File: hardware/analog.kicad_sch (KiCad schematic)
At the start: 23 parts

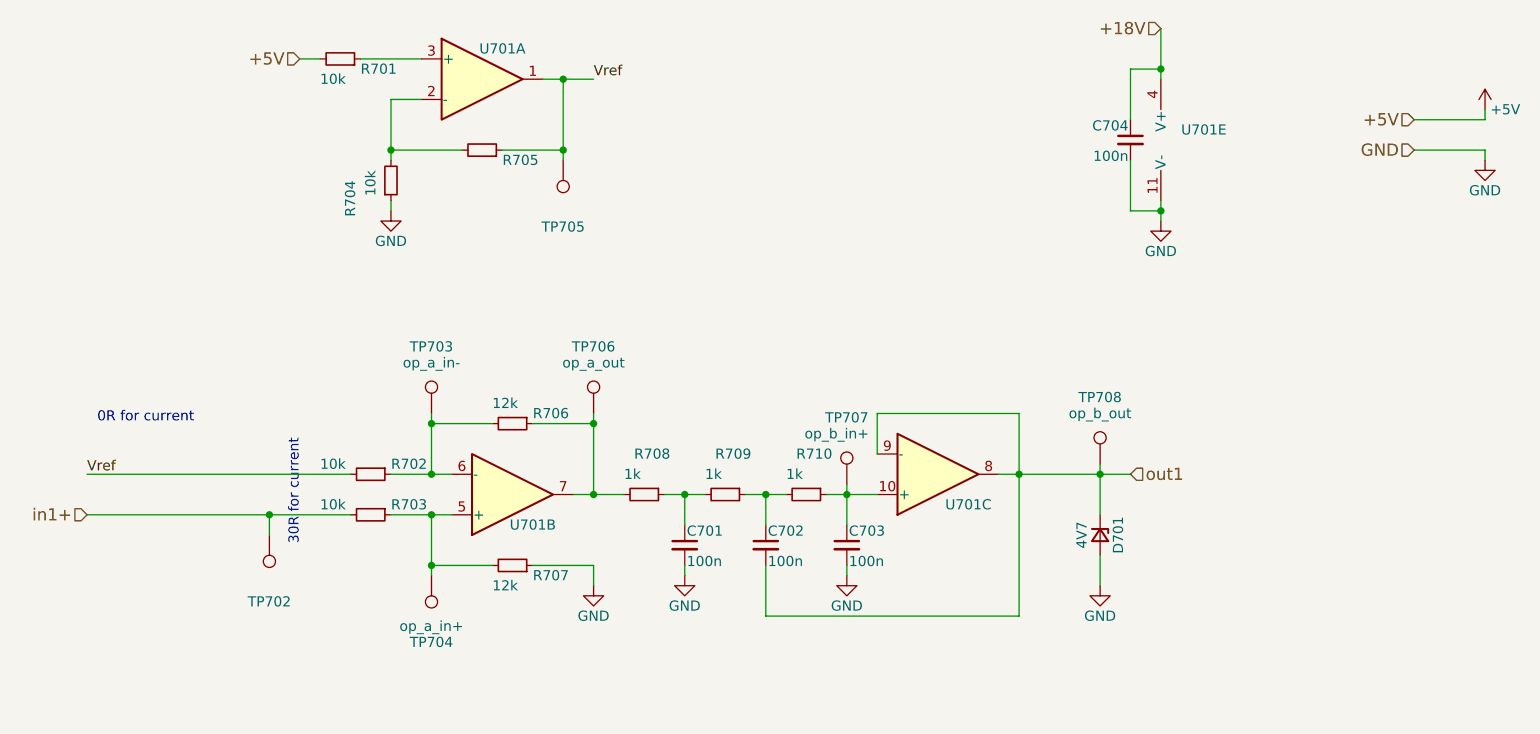
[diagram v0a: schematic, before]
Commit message: Adjusted analog, now using INA826. Simulations updated.
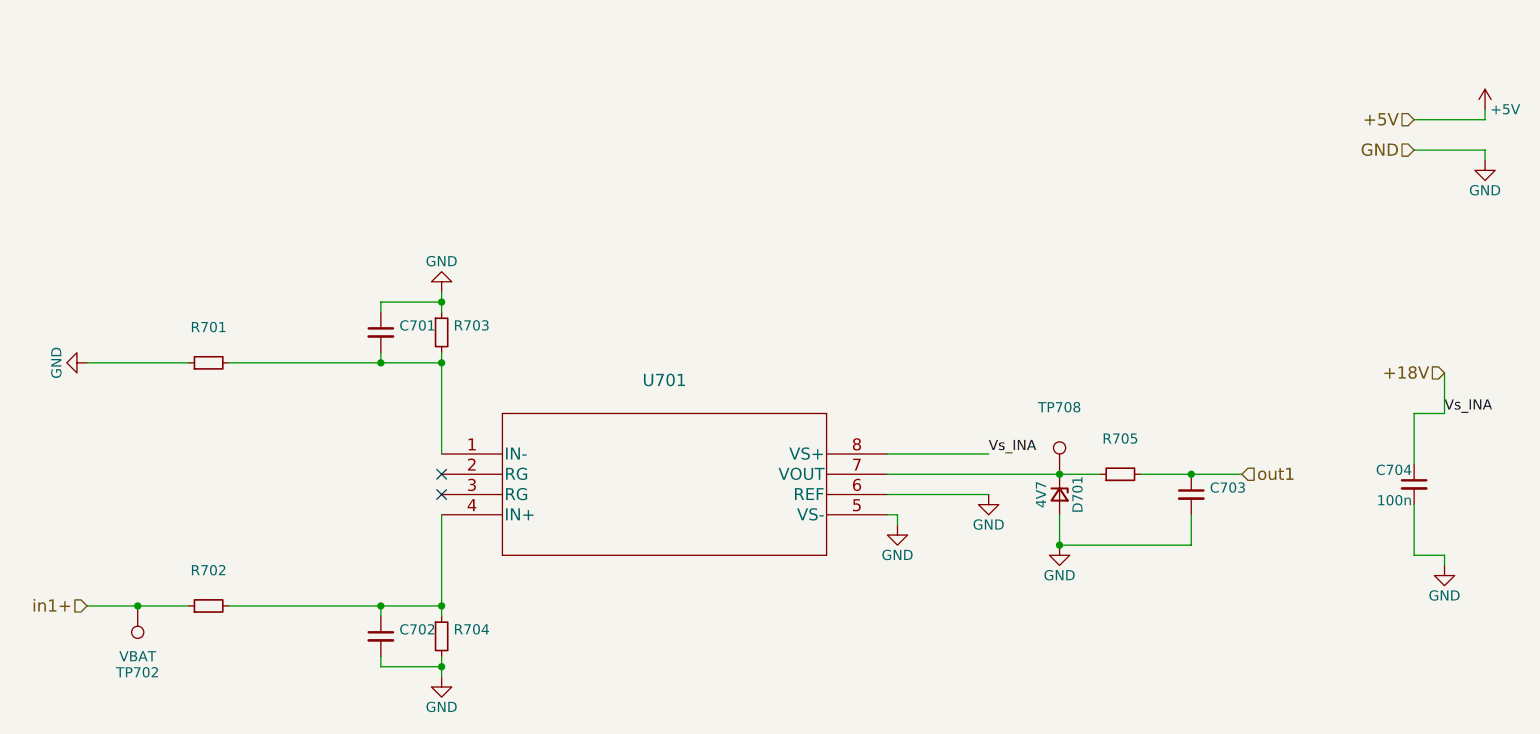
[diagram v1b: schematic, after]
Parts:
- removed R706, R707: 12k, symbol Device:R_Small
- removed R708, R709, R710: 1k, symbol Device:R_Small
- removed TP703: op_a_in-, TestPoint:TestPoint_Pad_2.0x2.0mm, symbol Connector:TestPoint
- removed TP704: op_a_in+, TestPoint:TestPoint_Pad_2.0x2.0mm, symbol Connector:TestPoint
- removed TP705: (no value), symbol Connector:TestPoint
- removed TP706: op_a_out, TestPoint:TestPoint_Pad_2.0x2.0mm, symbol Connector:TestPoint
- removed TP707: op_b_in+, TestPoint:TestPoint_Pad_2.0x2.0mm, symbol Connector:TestPoint
- removed U701: (no value), symbol Amplifier_Operational:LM324
- added U701: (no value), symbol INA826AIDR:INA826_D_8
- C701, C702, C703: value 100n -> (none)
- C704: footprint (none) -> Capacitor_SMD:C_0805_2012Metric_Pad1.18x1.45mm_HandSolder
- R701, R702, R703, R704: value 10k -> (none)
- TP702: value (none) -> VBAT; footprint (none) -> TestPoint:TestPoint_Pad_2.0x2.0mm
- TP708: value op_b_out -> (none); footprint TestPoint:TestPoint_Pad_2.0x2.0mm -> (none)
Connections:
- net +18V: now also U701.8 (VS+)
- net +5V: no longer R701.2
- net GND: now also C701.1, C702.2, R701.1, R703.1, R704.2, U701.5 (VS-), U701.6 (REF); no longer C701.2, R704.1
- net in1+: now also R702.1; no longer R703.2
- net out1: now also C703.1, R705.2; no longer C702.2, D701.1 (K), TP708.1
- net at C702.1: now also R702.2, R704.1, U701.4 (IN+)
- net Vref: no longer names the net of R705.1
- net Vref: now also D701.1 (K), TP708.1, U701.7 (VOUT); no longer R702.2
- new net: C701.2, R701.2, R703.2, U701.1 (IN-)
- no-connect marks 0 -> 2
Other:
- note removed: "0R for current"
- note removed: "30R for current"
- moved on the sheet: C704, D701, TP702, TP708

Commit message: Created BOM, removed Testpoints from it.
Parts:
- C701, C702: value (none) -> 1n; footprint (none) -> Capacitor_SMD:C_0805_2012Metric_Pad1.18x1.45mm_HandSolder
- C703: value (none) -> 1uF; footprint (none) -> Capacitor_SMD:C_1206_3216Metric_Pad1.33x1.80mm_HandSolder
- R701, R702: value (none) -> 22k; footprint (none) -> Resistor_SMD:R_0805_2012Metric_Pad1.20x1.40mm_HandSolder
- R703, R704: value (none) -> 8k2; footprint (none) -> Resistor_SMD:R_0805_2012Metric_Pad1.20x1.40mm_HandSolder
- R705: value (none) -> 100; footprint (none) -> Resistor_SMD:R_0805_2012Metric_Pad1.20x1.40mm_HandSolder
- TP708: value (none) -> out1; footprint (none) -> TestPoint:TestPoint_Pad_2.0x2.0mm
- U701: value (none) -> INA826_D_8; footprint (none) -> Package_SO:SOIC-8_3.9x4.9mm_P1.27mm
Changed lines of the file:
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@@
     (in_bom yes) (on_board yes) (fields_autoplaced)
     (property "Reference" "R702" (id 0) (at 91.44 113.6736 90))
-    (property "Value" "" (id 1) (at 91.44 116.2105 90))
-    (property "Footprint" "" (id 2) (at 91.44 118.11 0)
+    (property "Value" "22k" (id 1) (at 91.44 116.2105 90))
+    (property "Footprint" "Resistor_SMD:R_0805_2012Metric_Pad1.20x1.40mm_HandSolder" (id 2) (at 91.44 118.11 0)
       (effects (font (size 1.27 1.27)) hide)
     )
@@
       (effects (font (size 1.524 1.524)))
     )
-    (property "Value" "" (id 1) (at 148.59 92.8258 0)
+    (property "Value" "INA826_D_8" (id 1) (at 148.59 92.8258 0)
       (effects (font (size 1.524 1.524)))
     )
-    (property "Footprint" "" (id 2) (at 148.59 92.964 0)
+    (property "Footprint" "Package_SO:SOIC-8_3.9x4.9mm_P1.27mm" (id 2) (at 148.59 92.964 0)
       (effects (font (size 1.524 1.524)) hide)
     )
@@
       (effects (font (size 1.27 1.27)) (justify left))
     )
-    (property "Value" "" (id 1) (at 115.3541 123.6285 0)
-      (effects (font (size 1.27 1.27)) (justify left))
-    )
-    (property "Footprint" "" (id 2) (at 113.03 121.92 0)
+    (property "Value" "1n" (id 1) (at 115.3541 123.6285 0)
+      (effects (font (size 1.27 1.27)) (justify left))
+    )
+    (property "Footprint" "Capacitor_SMD:C_0805_2012Metric_Pad1.18x1.45mm_HandSolder" (id 2) (at 113.03 121.92 0)
       (effects (font (size 1.27 1.27)) hide)
     )
@@
       (effects (font (size 1.27 1.27)) (justify left))
     )
-    (property "Value" "" (id 1) (at 115.3541 85.5285 0)
-      (effects (font (size 1.27 1.27)) (justify left))
-    )
-    (property "Footprint" "" (id 2) (at 113.03 83.82 0)
+    (property "Value" "1n" (id 1) (at 115.3541 85.5285 0)
+      (effects (font (size 1.27 1.27)) (justify left))
+    )
+    (property "Footprint" "Capacitor_SMD:C_0805_2012Metric_Pad1.18x1.45mm_HandSolder" (id 2) (at 113.03 83.82 0)
       (effects (font (size 1.27 1.27)) hide)
     )
@@
       (effects (font (size 1.27 1.27)) (justify bottom))
     )
-    (property "Value" "" (id 1) (at 198.12 95.25 0))
-    (property "Footprint" "" (id 2) (at 198.12 101.6 0)
+    (property "Value" "out1" (id 1) (at 198.12 95.25 0))
+    (property "Footprint" "TestPoint:TestPoint_Pad_2.0x2.0mm" (id 2) (at 198.12 101.6 0)
       (effects (font (size 1.27 1.27)) hide)
     )
@@
     (in_bom yes) (on_board yes) (fields_autoplaced)
     (property "Reference" "R701" (id 0) (at 91.44 83.1936 90))
-    (property "Value" "" (id 1) (at 91.44 85.7305 90))
-    (property "Footprint" "" (id 2) (at 91.44 87.63 0)
+    (property "Value" "22k" (id 1) (at 91.44 85.7305 90))
+    (property "Footprint" "Resistor_SMD:R_0805_2012Metric_Pad1.20x1.40mm_HandSolder" (id 2) (at 91.44 87.63 0)
       (effects (font (size 1.27 1.27)) hide)
     )
@@
     (in_bom yes) (on_board yes) (fields_autoplaced)
     (property "Reference" "R705" (id 0) (at 205.74 97.1636 90))
-    (property "Value" "" (id 1) (at 205.74 99.7005 90))
-    (property "Footprint" "" (id 2) (at 205.74 101.6 0)
+    (property "Value" "100" (id 1) (at 205.74 99.7005 90))
+    (property "Footprint" "Resistor_SMD:R_0805_2012Metric_Pad1.20x1.40mm_HandSolder" (id 2) (at 205.74 101.6 0)
       (effects (font (size 1.27 1.27)) hide)
     )
@@
       (effects (font (size 1.27 1.27)) (justify left))
     )
-    (property "Value" "" (id 1) (at 216.9541 105.8485 0)
-      (effects (font (size 1.27 1.27)) (justify left))
-    )
-    (property "Footprint" "" (id 2) (at 214.63 104.14 0)
+    (property "Value" "1uF" (id 1) (at 216.9541 105.8485 0)
+      (effects (font (size 1.27 1.27)) (justify left))
+    )
+    (property "Footprint" "Capacitor_SMD:C_1206_3216Metric_Pad1.33x1.80mm_HandSolder" (id 2) (at 214.63 104.14 0)
       (effects (font (size 1.27 1.27)) hide)
     )
@@
       (effects (font (size 1.27 1.27)) (justify left))
     )
-    (property "Value" "" (id 1) (at 122.1486 123.6222 0)
-      (effects (font (size 1.27 1.27)) (justify left))
-    )
-    (property "Footprint" "" (id 2) (at 120.65 121.92 0)
+    (property "Value" "8k2" (id 1) (at 122.1486 123.6222 0)
+      (effects (font (size 1.27 1.27)) (justify left))
+    )
+    (property "Footprint" "Resistor_SMD:R_0805_2012Metric_Pad1.20x1.40mm_HandSolder" (id 2) (at 120.65 121.92 0)
       (effects (font (size 1.27 1.27)) hide)
     )
@@
       (effects (font (size 1.27 1.27)) (justify left))
     )
-    (property "Value" "" (id 1) (at 122.1486 85.5222 0)
-      (effects (font (size 1.27 1.27)) (justify left))
-    )
-    (property "Footprint" "" (id 2) (at 120.65 83.82 0)
-      (effects (font (size 1.27 1.27)) hide)
-    )
+    (property "Value" "8k2" (id 1) (at 122.1486 85.5222 0)
+      (effects (font (size 1.27 1.27)) (justify left))
+    )
+    (property "Footprint" "Resistor_SMD:R_0805_2012Metric_Pad1.20x1.40mm_HandSolder" (id 2) (at 120.65 83.82 0)
+      (effects (font (size 1.27 1.27)) hide)
+    )
